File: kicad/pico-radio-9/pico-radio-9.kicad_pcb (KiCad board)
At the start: 2 copper layers, 87.2 x 67 mm, 49 parts, among them J1 HF Amplifier, J2 MW/SW antenna, J3 FM antenna, J4 SW antenna, J5 Batterry, Q1 PN2222A, Q2 PN2222A, Q3 PN2222A, SW1 Reset, U1 SI4732-A10-GS, U2 TFT_320x240, U3 KY-040, Y1 32.762kHz

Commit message: HWSW mutestat + kicad file rename
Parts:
- JP3: value TFT SDO -> TFT SDO - ha kell
- R3, R4: value 22k -> 1k
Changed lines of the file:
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@@
 	(paper "A5" portrait)
 	(title_block
-		(title "Pico Radio 5")
+		(title "Pico Radio 9")
 	)
 	(layers
@@
 		(property ki_fp_filters "TO?92*")
 		(sheetname "/")
-		(sheetfile "pico-radio-5.kicad_sch")
+		(sheetfile "pico-radio-9.kicad_sch")
 		(attr through_hole)
 		(fp_line
@@
 		(property ki_fp_filters "Choke_* *Coil* Inductor_* L_*")
 		(sheetname "/")
-		(sheetfile "pico-radio-5.kicad_sch")
+		(sheetfile "pico-radio-9.kicad_sch")
 		(attr through_hole)
 		(fp_line
@@
 		(property ki_fp_filters "C_*")
 		(sheetname "/")
-		(sheetfile "pico-radio-5.kicad_sch")
+		(sheetfile "pico-radio-9.kicad_sch")
 		(attr through_hole)
 		(fp_line
@@
 		(property ki_fp_filters "CP_*")
 		(sheetname "/")
-		(sheetfile "pico-radio-5.kicad_sch")
+		(sheetfile "pico-radio-9.kicad_sch")
 		(attr through_hole)
 		(fp_line
@@
 		(property ki_fp_filters "SW*Omron*B3FS*")
 		(sheetname "/")
-		(sheetfile "pico-radio-5.kicad_sch")
+		(sheetfile "pico-radio-9.kicad_sch")
 		(attr through_hole)
 		(fp_line
@@
 		(property ki_fp_filters "Connector*:*_1x??_*")
 		(sheetname "/")
-		(sheetfile "pico-radio-5.kicad_sch")
+		(sheetfile "pico-radio-9.kicad_sch")
 		(attr through_hole)
 		(fp_line
@@
 			)
 		)
-		(property "Value" "22k"
+		(property "Value" "1k"
 			(at 5.08 2.37 90)
 			(layer "F.Fab")
@@
 		(property ki_fp_filters "R_*")
 		(sheetname "/")
-		(sheetfile "pico-radio-5.kicad_sch")
+		(sheetfile "pico-radio-9.kicad_sch")
 		(attr through_hole)
 		(fp_line
@@
 		(property ki_fp_filters "CP_*")
 		(sheetname "/")
-		(sheetfile "pico-radio-5.kicad_sch")
+		(sheetfile "pico-radio-9.kicad_sch")
 		(attr through_hole)
 		(fp_line
@@
 		(property ki_fp_filters "Choke_* *Coil* Inductor_* L_*")
 		(sheetname "/")
-		(sheetfile "pico-radio-5.kicad_sch")
+		(sheetfile "pico-radio-9.kicad_sch")
 		(attr through_hole)
 		(fp_line
@@
 			)
 		)
-		(property "Value" "22k"
+		(property "Value" "1k"
 			(at 5.08 2.37 90)
 			(layer "F.Fab")
@@
 		(property ki_fp_filters "R_*")
 		(sheetname "/")
-		(sheetfile "pico-radio-5.kicad_sch")
+		(sheetfile "pico-radio-9.kicad_sch")
 		(attr through_hole)
 		(fp_line
@@
 		(property ki_fp_filters "Jumper* TestPoint*2Pads* TestPoint*Bridge*")
 		(sheetname "/")
-		(sheetfile "pico-radio-5.kicad_sch")
+		(sheetfile "pico-radio-9.kicad_sch")
 		(attr through_hole)
 		(fp_line
@@
 		(property ki_fp_filters "R_*")
 		(sheetname "/")
-		(sheetfile "pico-radio-5.kicad_sch")
+		(sheetfile "pico-radio-9.kicad_sch")
 		(attr through_hole)
 		(fp_line
@@
 		(property ki_fp_filters "C_*")
 		(sheetname "/")
-		(sheetfile "pico-radio-5.kicad_sch")
+		(sheetfile "pico-radio-9.kicad_sch")
 		(attr through_hole)
 		(fp_line
@@
 		(property ki_fp_filters "R_*")
 		(sheetname "/")
-		(sheetfile "pico-radio-5.kicad_sch")
+		(sheetfile "pico-radio-9.kicad_sch")
 		(attr through_hole)
 		(fp_line
@@
 		(property ki_fp_filters "C_*")
 		(sheetname "/")
-		(sheetfile "pico-radio-5.kicad_sch")
+		(sheetfile "pico-radio-9.kicad_sch")
 		(attr through_hole)
 		(fp_line
@@
 		)
 		(sheetname "/")
-		(sheetfile "pico-radio-5.kicad_sch")
+		(sheetfile "pico-radio-9.kicad_sch")
 		(attr through_hole)
 		(fp_line
@@
 		(property ki_fp_filters "TerminalBlock*:*")
 		(sheetname "/")
-		(sheetfile "pico-radio-5.kicad_sch")
+		(sheetfile "pico-radio-9.kicad_sch")
 		(attr through_hole)
 		(fp_line
@@
 		(property ki_fp_filters "R_*")
 		(sheetname "/")
-		(sheetfile "pico-radio-5.kicad_sch")
+		(sheetfile "pico-radio-9.kicad_sch")
 		(attr through_hole)
 		(fp_line
@@
 		(property ki_fp_filters "R_*")
 		(sheetname "/")
-		(sheetfile "pico-radio-5.kicad_sch")
+		(sheetfile "pico-radio-9.kicad_sch")
 		(attr through_hole)
 		(fp_line
@@
 		(property ki_fp_filters "TO?92*")
 		(sheetname "/")
-		(sheetfile "pico-radio-5.kicad_sch")
+		(sheetfile "pico-radio-9.kicad_sch")
 		(attr through_hole)
 		(fp_line
@@
 		(property ki_fp_filters "Connector*:*_1x??_*")
 		(sheetname "/")
-		(sheetfile "pico-radio-5.kicad_sch")
+		(sheetfile "pico-radio-9.kicad_sch")
 		(attr through_hole)
 		(fp_line
@@
 		(property ki_fp_filters "Crystal*")
 		(sheetname "/")
-		(sheetfile "pico-radio-5.kicad_sch")
+		(sheetfile "pico-radio-9.kicad_sch")
 		(attr through_hole)
 		(fp_line
@@
 		(property ki_fp_filters "R_*")
 		(sheetname "/")
-		(sheetfile "pico-radio-5.kicad_sch")
+		(sheetfile "pico-radio-9.kicad_sch")
 		(attr through_hole)
 		(fp_line
@@
 		(property ki_fp_filters "Connector*:*_1x??_*")
 		(sheetname "/")
-		(sheetfile "pico-radio-5.kicad_sch")
+		(sheetfile "pico-radio-9.kicad_sch")
 		(attr through_hole)
 		(fp_line
@@
 		(property ki_fp_filters "C_*")
 		(sheetname "/")
-		(sheetfile "pico-radio-5.kicad_sch")
+		(sheetfile "pico-radio-9.kicad_sch")
 		(attr through_hole)
 		(fp_line
@@
 		(property ki_fp_filters "Choke_* *Coil* Inductor_* L_*")
 		(sheetname "/")
-		(sheetfile "pico-radio-5.kicad_sch")
+		(sheetfile "pico-radio-9.kicad_sch")
 		(attr through_hole)
 		(fp_line
@@
 		(property ki_fp_filters "R_*")
 		(sheetname "/")
-		(sheetfile "pico-radio-5.kicad_sch")
+		(sheetfile "pico-radio-9.kicad_sch")
 		(attr through_hole)
 		(fp_line
@@
 		(property ki_fp_filters "Choke_* *Coil* Inductor_* L_*")
 		(sheetname "/")
-		(sheetfile "pico-radio-5.kicad_sch")
+		(sheetfile "pico-radio-9.kicad_sch")
 		(attr through_hole)
 		(fp_line
@@
 		(property ki_fp_filters "TerminalBlock*:*")
 		(sheetname "/")
-		(sheetfile "pico-radio-5.kicad_sch")
+		(sheetfile "pico-radio-9.kicad_sch")
 		(attr through_hole)
 		(fp_line
@@
 		(property ki_fp_filters "TO?92*")
 		(sheetname "/")
-		(sheetfile "pico-radio-5.kicad_sch")
+		(sheetfile "pico-radio-9.kicad_sch")
 		(attr through_hole)
 		(fp_line
@@
 		(property ki_fp_filters "R_*")
 		(sheetname "/")
-		(sheetfile "pico-radio-5.kicad_sch")
+		(sheetfile "pico-radio-9.kicad_sch")
 		(attr through_hole)
 		(fp_line
@@
 		(property ki_fp_filters "CP_*")
 		(sheetname "/")
-		(sheetfile "pico-radio-5.kicad_sch")
+		(sheetfile "pico-radio-9.kicad_sch")
 		(attr through_hole)
 		(fp_line
@@
 		(property ki_fp_filters "C_*")
 		(sheetname "/")
-		(sheetfile "pico-radio-5.kicad_sch")
+		(sheetfile "pico-radio-9.kicad_sch")
 		(attr through_hole)
 		(fp_line
@@
 		)
 		(sheetname "/")
-		(sheetfile "pico-radio-5.kicad_sch")
+		(sheetfile "pico-radio-9.kicad_sch")
 		(attr through_hole)
 		(fp_line
@@
 		(property ki_fp_filters "R_*")
 		(sheetname "/")
-		(sheetfile "pico-radio-5.kicad_sch")
+		(sheetfile "pico-radio-9.kicad_sch")
 		(attr through_hole)
 		(fp_line
@@
 		(property ki_fp_filters "RaspberryPi?Pico?Common* RaspberryPi?Pico?SMD*")
 		(sheetname "/")
-		(sheetfile "pico-radio-5.kicad_sch")
+		(sheetfile "pico-radio-9.kicad_sch")
 		(attr through_hole)
 		(fp_line
@@
 		(property ki_fp_filters "C_*")
 		(sheetname "/")
-		(sheetfile "pico-radio-5.kicad_sch")
+		(sheetfile "pico-radio-9.kicad_sch")
 		(attr through_hole)
 		(fp_line
@@
 		(property ki_fp_filters "*Buzzer*")
 		(sheetname "/")
-		(sheetfile "pico-radio-5.kicad_sch")
+		(sheetfile "pico-radio-9.kicad_sch")
 		(attr through_hole)
 		(fp_circle
@@
 		(property ki_fp_filters "CP_*")
 		(sheetname "/")
-		(sheetfile "pico-radio-5.kicad_sch")
+		(sheetfile "pico-radio-9.kicad_sch")
 		(attr through_hole)
 		(fp_line
@@
 		(property ki_fp_filters "C_*")
 		(sheetname "/")
-		(sheetfile "pico-radio-5.kicad_sch")
+		(sheetfile "pico-radio-9.kicad_sch")
 		(attr through_hole)
 		(fp_line
@@
 		(property ki_fp_filters "C_*")
 		(sheetname "/")
-		(sheetfile "pico-radio-5.kicad_sch")
+		(sheetfile "pico-radio-9.kicad_sch")
 		(attr through_hole)
 		(fp_line
@@
 		(property ki_fp_filters "R_*")
 		(sheetname "/")
-		(sheetfile "pico-radio-5.kicad_sch")
+		(sheetfile "pico-radio-9.kicad_sch")
 		(attr through_hole)
 		(fp_line
@@
 		(property ki_fp_filters "SOIC_A10-GS_SIL SOIC_A10-GS_SIL-M SOIC_A10-GS_SIL-L")
 		(sheetname "/")
-		(sheetfile "pico-radio-5.kicad_sch")
+		(sheetfile "pico-radio-9.kicad_sch")
 		(attr smd)
 		(fp_line
@@
 		(property ki_fp_filters "SolderJumper*Bridged12*")
 		(sheetname "/")
-		(sheetfile "pico-radio-5.kicad_sch")
+		(sheetfile "pico-radio-9.kicad_sch")
 		(zone_connect 1)
 		(attr exclude_from_pos_files exclude_from_bom allow_soldermask_bridges)
@@
 			)
 		)
-		(property "Value" "TFT SDO"
+		(property "Value" "TFT SDO - ha kell"
 			(at 0 -1.9 90)
 			(layer "B.Fab")
@@
 		(property ki_fp_filters "SolderJumper*Open*")
 		(sheetname "/")
-		(sheetfile "pico-radio-5.kicad_sch")
+		(sheetfile "pico-radio-9.kicad_sch")
 		(zone_connect 1)
 		(attr exclude_from_pos_files exclude_from_bom allow_soldermask_bridges)

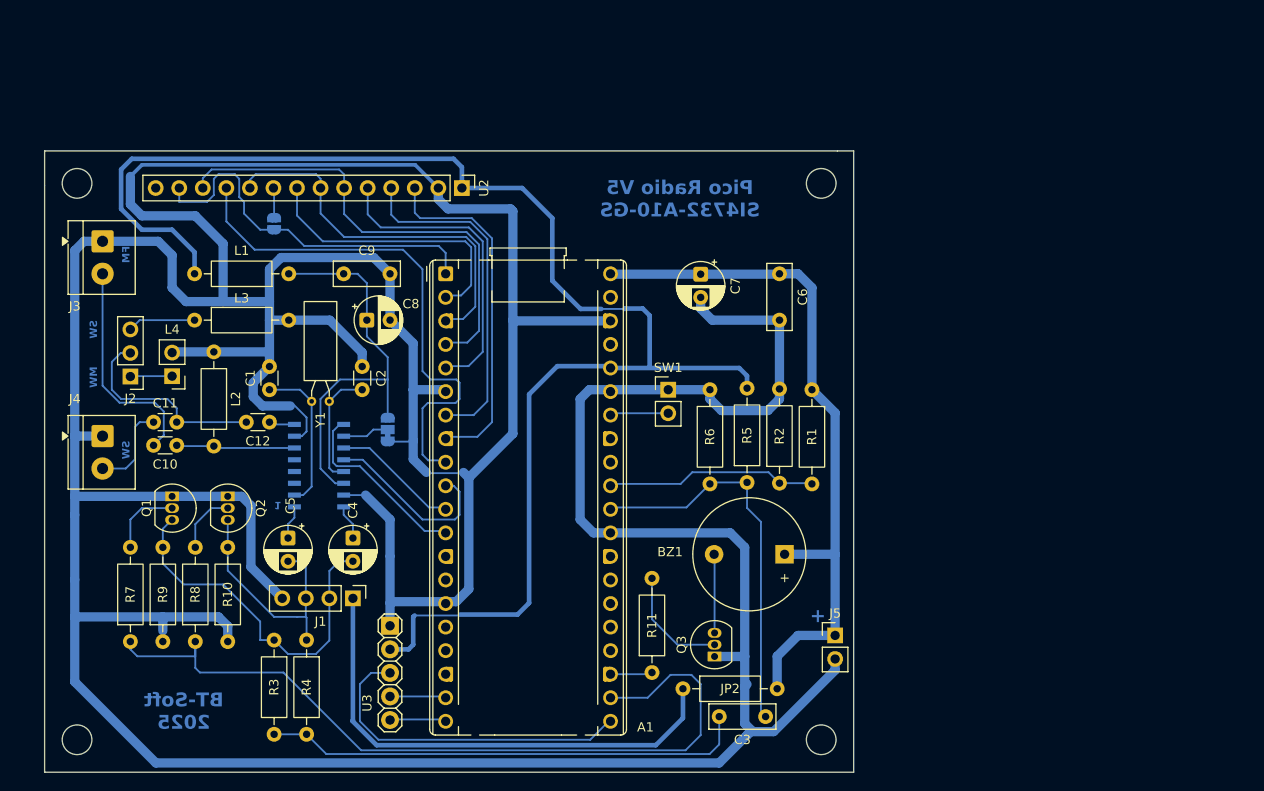
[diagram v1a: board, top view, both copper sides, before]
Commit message: Add UICompTuningBar component for spectrum visualization
- Implemented UICompTuningBar class to display a tuning bar for frequency spectrum analysis.
- Added methods for updating spectrum data, drawing the tuning bar, and managing frequency markers.
- Integrated peak hold logic for better visualization of signal strength over time.
- Included color coding for bar heights based on magnitude.
- Optimized rendering with sprite support for improved performance.
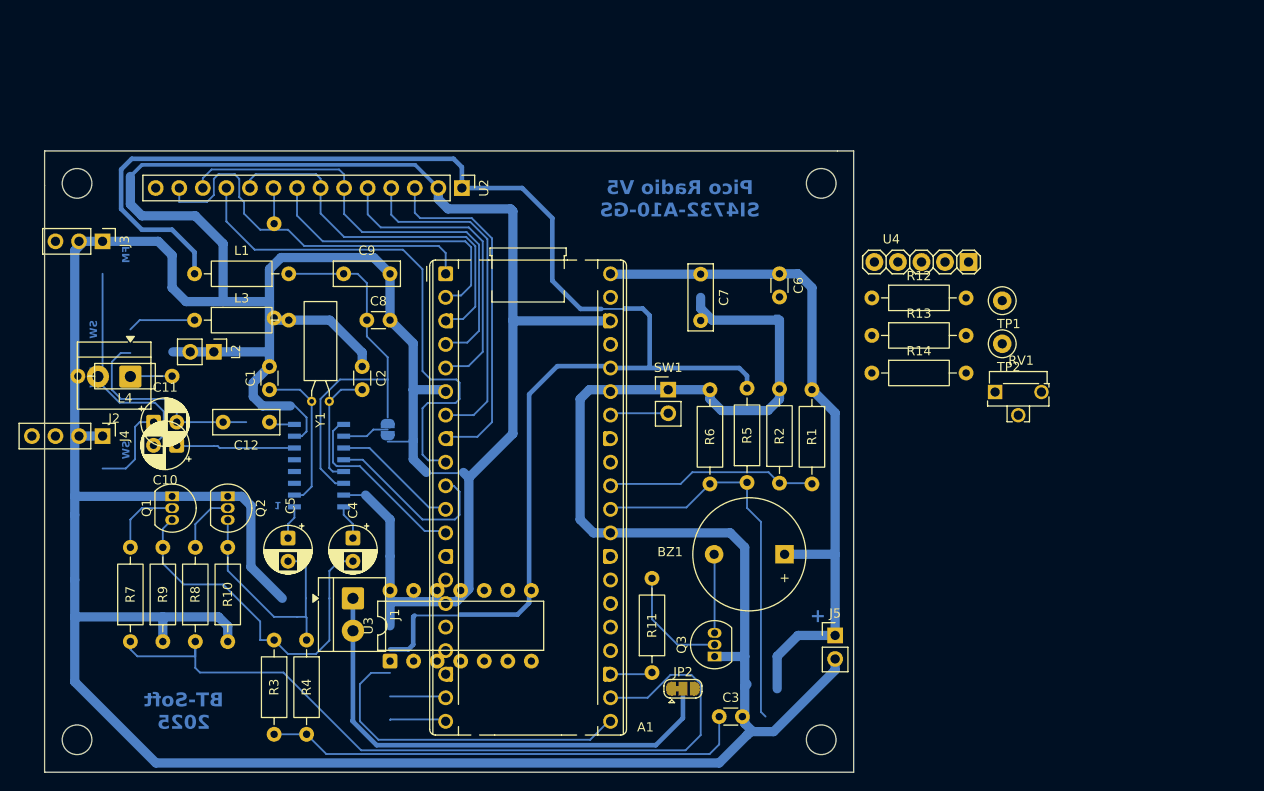
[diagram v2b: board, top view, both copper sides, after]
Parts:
- added R12: 10k, Resistor_THT:R_Axial_DIN0207_L6.3mm_D2.5mm_P10.16mm_Horizontal, F.Cu at (118.0, 56.1)
- added R13: 15k, Resistor_THT:R_Axial_DIN0207_L6.3mm_D2.5mm_P10.16mm_Horizontal, F.Cu at (118.0, 60.1)
- added R14: 4.7k, Resistor_THT:R_Axial_DIN0207_L6.3mm_D2.5mm_P10.16mm_Horizontal, F.Cu at (118.0, 64.2)
- added RV1: 47k, Potentiometer_THT:Potentiometer_Runtron_RM-063_Horizontal, F.Cu at (131.2, 66.2)
- added TP1: Jelgenerátorból, TestPoint:TestPoint_Loop_D2.50mm_Drill1.0mm, F.Cu at (132.0, 56.4)
- added TP2: Oszcilloszkópra, TestPoint:TestPoint_Loop_D2.50mm_Drill1.0mm, F.Cu at (132.0, 61.0)
- added U4: KY-040, Rotary_Encoder:KY-040-PORT, F.Cu at (124.6, 52.2)
- C1: value 22pF -> 33pF
- C10: value 33pF -> 4.7uF; footprint Capacitor_THT:C_Disc_D3.0mm_W1.6mm_P2.50mm -> Capacitor_THT:CP_Radial_D5.0mm_P2.50mm
- C11: value 1nF -> 4.7uF; footprint Capacitor_THT:C_Disc_D3.0mm_W1.6mm_P2.50mm -> Capacitor_THT:CP_Radial_D5.0mm_P2.50mm
- C12: value 1nF -> 100nF; footprint Capacitor_THT:C_Disc_D3.0mm_W1.6mm_P2.50mm -> Capacitor_THT:C_Disc_D7.0mm_W2.5mm_P5.00mm
- C2: value 22pF -> 1nF
- C3: value 100nF -> 1nF; footprint Capacitor_THT:C_Disc_D7.0mm_W2.5mm_P5.00mm -> Capacitor_THT:C_Disc_D3.0mm_W1.6mm_P2.50mm
- C6: value 100nF -> 22pF; footprint Capacitor_THT:C_Disc_D7.0mm_W2.5mm_P5.00mm -> Capacitor_THT:C_Disc_D3.0mm_W1.6mm_P2.50mm
- C7: value 4.7uF -> 100nF; footprint Capacitor_THT:CP_Radial_D5.0mm_P2.50mm -> Capacitor_THT:C_Disc_D7.0mm_W2.5mm_P5.00mm
- C8: value 4.7uF -> 22pF; footprint Capacitor_THT:CP_Radial_D5.0mm_P2.50mm -> Capacitor_THT:C_Disc_D3.0mm_W1.6mm_P2.50mm
- J1: value HF Amplifier -> FM antenna; footprint Connector_PinHeader_2.54mm:PinHeader_1x04_P2.54mm_Vertical -> TerminalBlock_4Ucon:TerminalBlock_4Ucon_1x02_P3.50mm_Horizontal
- J2: value MW/SW antenna -> SW antenna; footprint Connector_PinHeader_2.54mm:PinHeader_1x03_P2.54mm_Vertical -> TerminalBlock_4Ucon:TerminalBlock_4Ucon_1x02_P3.50mm_Horizontal
- J3: value FM antenna -> MW/SW antenna; footprint TerminalBlock_4Ucon:TerminalBlock_4Ucon_1x02_P3.50mm_Horizontal -> Connector_PinHeader_2.54mm:PinHeader_1x03_P2.54mm_Vertical
- J4: value SW antenna -> HF Amplifier; footprint TerminalBlock_4Ucon:TerminalBlock_4Ucon_1x02_P3.50mm_Horizontal -> Connector_PinHeader_2.54mm:PinHeader_1x04_P2.54mm_Vertical
- JP1: value Si4732 I2C Address -> TFT SDO - ha kell; footprint Jumper:SolderJumper-3_P1.3mm_Bridged12_RoundedPad1.0x1.5mm -> Jumper:SolderJumper-2_P1.3mm_Open_RoundedPad1.0x1.5mm
- JP2: value NYÁK átkötés -> Si4732 I2C Address; footprint Resistor_THT:R_Axial_DIN0207_L6.3mm_D2.5mm_P10.16mm_Horizontal -> Jumper:SolderJumper-3_P1.3mm_Bridged12_RoundedPad1.0x1.5mm
- JP3: value TFT SDO - ha kell -> NYÁK átkötés; footprint Jumper:SolderJumper-2_P1.3mm_Open_RoundedPad1.0x1.5mm -> Resistor_THT:R_Axial_DIN0207_L6.3mm_D2.5mm_P10.16mm_Horizontal
- L1: value 220uH -> 47uH
- L2: value 220uH -> 30uH (MW Ferrite antenna); footprint Resistor_THT:R_Axial_DIN0207_L6.3mm_D2.5mm_P10.16mm_Horizontal -> Connector_PinHeader_2.54mm:PinHeader_1x02_P2.54mm_Vertical
- L3: value 47uH -> 220uH
- L4: value 30uH (MW Ferrite antenna) -> 220uH; footprint Connector_PinHeader_2.54mm:PinHeader_1x02_P2.54mm_Vertical -> Resistor_THT:R_Axial_DIN0207_L6.3mm_D2.5mm_P10.16mm_Horizontal
- R1: value 10k -> 4.7k
- R10, R9: value 4.7k -> 47k
- R11, R8: value 4.7k -> 100k
- R2: value 15k -> 4.7k
- R3, R4: value 1k -> 4.7k
- R7: value 4.7k -> 10k
- U3: value KY-040 -> MCP6004; footprint Rotary_Encoder:KY-040-PORT -> Package_DIP:DIP-14_W7.62mm
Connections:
- C1 pad 1: Net-(U1-GPO3/DCLK) -> Net-(U1-FMI)
- C1 pad 2: GND -> Net-(J1-Pin_2)
- C10 pad 1: Net-(U1-FMI) -> Net-(JP2-B)
- C10 pad 2: Net-(J3-Pin_2) -> GND
- C11 pad 1: Net-(J4-Pin_2) -> +Vbus
- C11 pad 2: Net-(J2-Pin_2) -> GND
- C12 pad 1: Net-(U1-AMI) -> +Vbus
- C12 pad 2: Net-(J2-Pin_2) -> GND
- C2 pad 1: GND -> Net-(J2-Pin_2)
- C2 pad 2: Net-(U1-RCLK) -> Net-(J3-Pin_2)
- C3 pad 1: Net-(C3-Pad1) -> Net-(U1-AMI)
- C3 pad 2: AD_FFT_AUDIO -> Net-(J3-Pin_2)
- C6 pad 1: +Vbus -> Net-(U1-GPO3/DCLK)
- C7 pad 1: +Vbus -> Net-(C7-Pad1)
- C7 pad 2: GND -> Net-(C7-Pad2)
- C8 pad 1: Net-(JP1-B) -> GND
- C8 pad 2: GND -> Net-(U1-RCLK)
- C9 pad 2: Net-(JP1-B) -> Net-(JP2-B)
- J1 pad 1: Net-(J1-Pin_1) -> GND
- J1 pad 2: AUDIO_R -> Net-(J1-Pin_2)
- J2 pad 1: Net-(J2-Pin_1) -> GND
- J3 pad 1: GND -> Net-(J3-Pin_1)
- J4 pad 1: GND -> Net-(J4-Pin_1)
- J4 pad 2: Net-(J4-Pin_2) -> AUDIO_R
- JP1 pad 1: GND -> Net-(JP1-A)
- JP1 pad 2: Net-(JP1-C) -> /SDO
- JP2 pad 1: Net-(J1-Pin_1) -> GND
- JP2 pad 2: +Vbus -> Net-(JP2-C)
- JP3 pad 1: Net-(JP3-A) -> Net-(J4-Pin_1)
- JP3 pad 2: /SDO -> +Vbus
- L1 pad 1: Net-(JP1-B) -> Net-(J3-Pin_3)
- L1 pad 2: +3.3V -> GND
- L2 pad 1: GND -> Net-(J3-Pin_1)
- L2 pad 2: Net-(U1-FMI) -> GND
- L3 pad 1: Net-(J2-Pin_3) -> GND
- L3 pad 2: GND -> Net-(U1-FMI)
- L4 pad 1: Net-(J2-Pin_1) -> Net-(JP2-B)
- L4 pad 2: GND -> +3.3V
- R1 pad 1: +Vbus -> AUDIO_MUTE
- R1 pad 2: Net-(A1-GPIO27_ADC1) -> Net-(Q1-B)
- R10 pad 2: AUDIO_L -> Net-(U3A-+)
- R11 pad 1: BUZZER -> Net-(R11-Pad1)
- R11 pad 2: Net-(Q3-B) -> Net-(U3A--)
- R2 pad 1: Net-(A1-GPIO27_ADC1) -> AUDIO_MUTE
- R2 pad 2: GND -> Net-(Q2-B)
- R3 pad 1: AUDIO_R -> GND
- R3 pad 2: Net-(C3-Pad1) -> AUDIO_R
- R4 pad 1: AUDIO_L -> GND
- R4 pad 2: Net-(C3-Pad1) -> AUDIO_L
- R5 pad 1: AD_FFT_AUDIO -> Net-(U3A--)
- R5 pad 2: +3.3V -> AUDIO_R
- R6 pad 1: GND -> Net-(U3A--)
- R6 pad 2: AD_FFT_AUDIO -> Net-(C7-Pad1)
- R7 pad 1: AUDIO_MUTE -> Net-(U3A--)
- R7 pad 2: Net-(Q1-B) -> AUDIO_L
- R8 pad 1: AUDIO_MUTE -> Net-(U3A-+)
- R8 pad 2: Net-(Q2-B) -> Net-(U3A--)
- R9 pad 1: GND -> Net-(U3A-+)
- R9 pad 2: AUDIO_R -> +3.3V
- U1 pad 10: Net-(JP1-C) -> Net-(JP2-C)
- U1 pad 14: Net-(JP1-B) -> Net-(JP2-B)
- U2 pad 9: Net-(JP3-A) -> Net-(JP1-A)
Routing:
- net GND: track 561.0 -> 590.5 mm
- net Net-(J2-Pin_2): track 22.2 -> 0.00 mm
- net +Vbus: track 77.0 -> 86.7 mm
- net Net-(J4-Pin_2): track 9.62 -> 0.00 mm
- net Net-(J2-Pin_3): track 7.33 -> 0.00 mm
- net Net-(JP2-C): track 0.00 -> 5.05 mm
- net Net-(JP1-C): track 5.05 -> 0.00 mm
